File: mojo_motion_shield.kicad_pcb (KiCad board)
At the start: 2 copper layers, 63.5 x 78.7 mm, 1 part, among them P1 MOJO

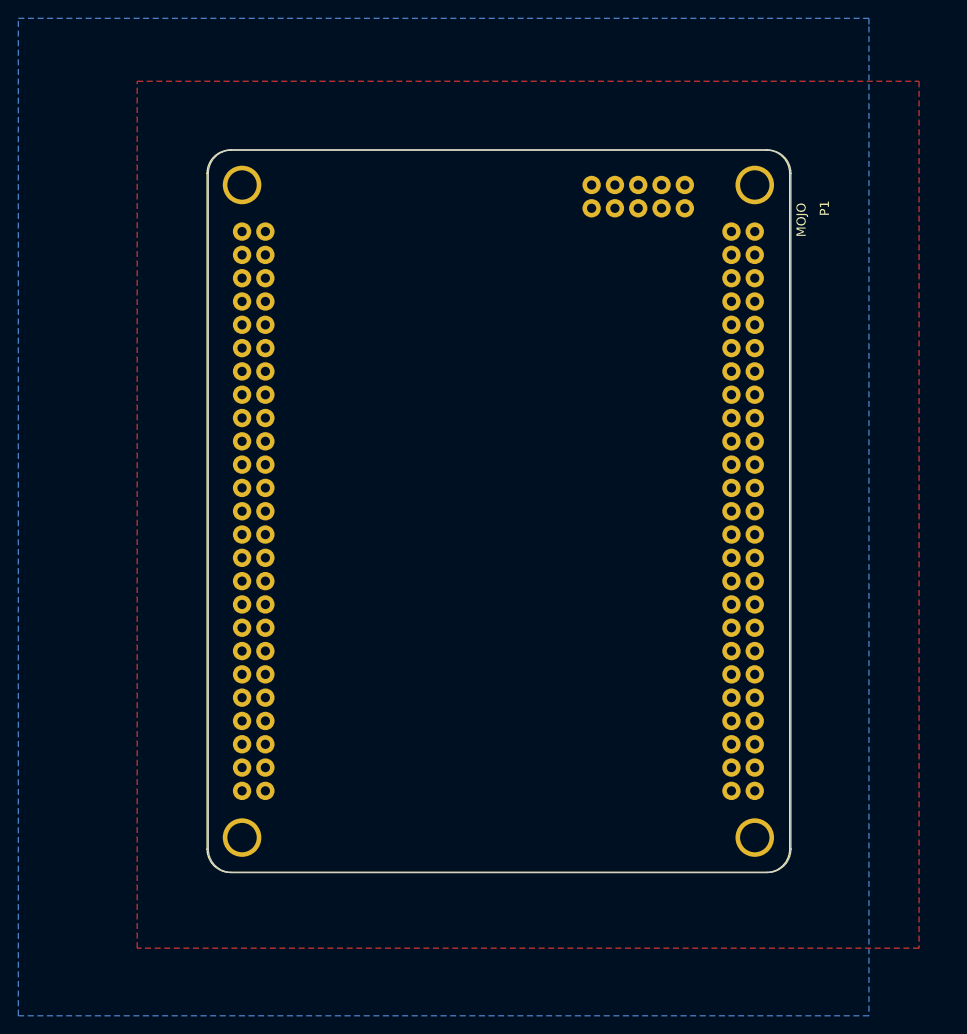
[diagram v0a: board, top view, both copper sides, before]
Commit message: flesh out pcb layout
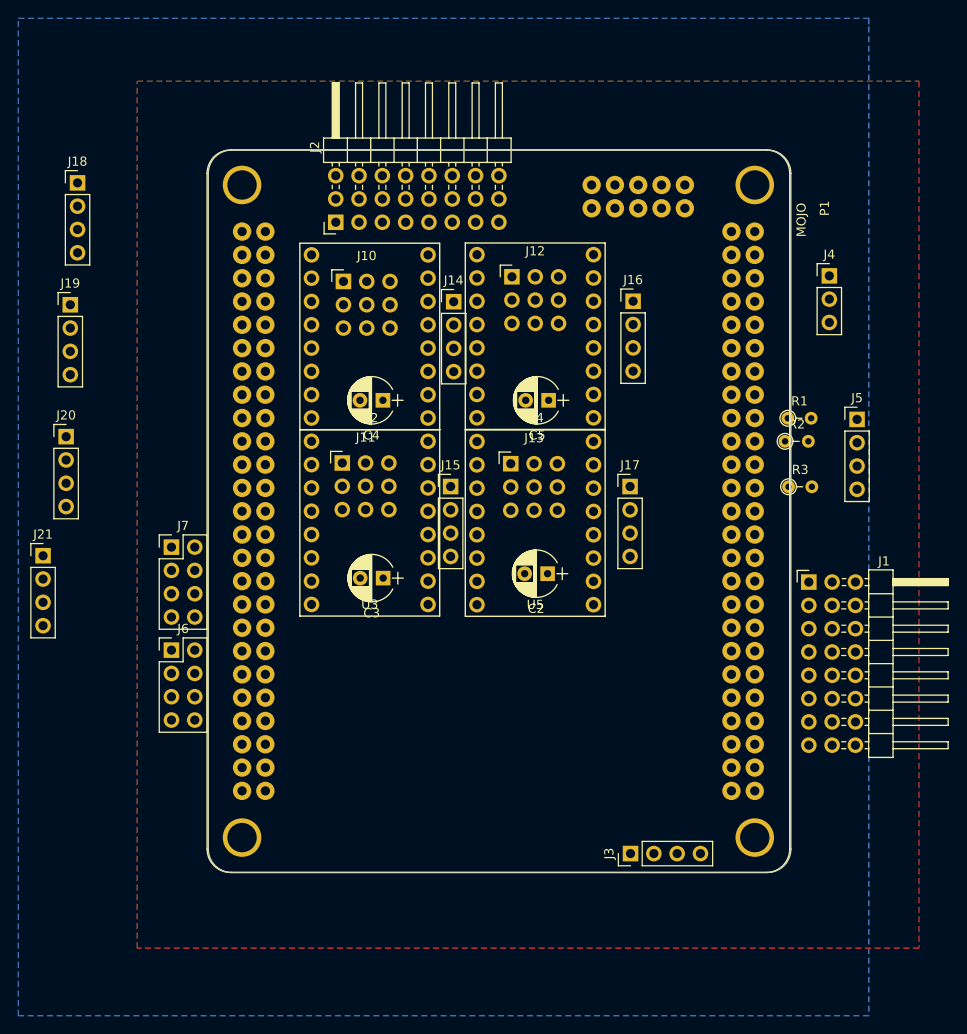
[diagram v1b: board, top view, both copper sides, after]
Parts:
- added C2: CP_Small, Capacitors_THT:CP_Radial_D5.0mm_P2.50mm, F.Cu at (148.7, 105.1)
- added C3: CP_Small, Capacitors_THT:CP_Radial_D5.0mm_P2.50mm, F.Cu at (130.8, 105.6)
- added C4: CP_Small, Capacitors_THT:CP_Radial_D5.0mm_P2.50mm, F.Cu at (130.8, 86.2)
- added C5: CP_Small, Capacitors_THT:CP_Radial_D5.0mm_P2.50mm, F.Cu at (148.9, 86.2)
- added J1: Conn_01x24, mojov3:Pin_Header_Angled_3x08_Pitch2.54mm, F.Cu at (179.8, 106.0)
- added J10: Conn_01x09, mojov3:Pin_Header_Straight_3x03_Pitch2.54mm, F.Cu at (129.0, 73.3)
- added J11: Conn_01x09, mojov3:Pin_Header_Straight_3x03_Pitch2.54mm, F.Cu at (128.9, 93.0)
- added J12: Conn_01x09, mojov3:Pin_Header_Straight_3x03_Pitch2.54mm, F.Cu at (147.4, 72.7)
- added J13: Conn_01x09, mojov3:Pin_Header_Straight_3x03_Pitch2.54mm, F.Cu at (147.3, 93.1)
- added J14: Conn_01x04, Pin_Headers:Pin_Header_Straight_1x04_Pitch2.54mm, F.Cu at (138.5, 75.5)
- added J15: Conn_01x04, Pin_Headers:Pin_Header_Straight_1x04_Pitch2.54mm, F.Cu at (138.2, 95.6)
- added J16: Conn_01x04, Pin_Headers:Pin_Header_Straight_1x04_Pitch2.54mm, F.Cu at (158.1, 75.4)
- added J17: Conn_01x04, Pin_Headers:Pin_Header_Straight_1x04_Pitch2.54mm, F.Cu at (157.7, 95.6)
- added J18: Conn_01x04, Pin_Headers:Pin_Header_Straight_1x04_Pitch2.54mm, F.Cu at (97.5, 62.5)
- added J19: Conn_01x04, Pin_Headers:Pin_Header_Straight_1x04_Pitch2.54mm, F.Cu at (96.7, 75.8)
- added J2: Conn_01x24, mojov3:Pin_Header_Angled_3x08_Pitch2.54mm, F.Cu at (125.7, 64.3)
- added J20: Conn_01x04, Pin_Headers:Pin_Header_Straight_1x04_Pitch2.54mm, F.Cu at (96.3, 90.2)
- added J21: Conn_01x04, Pin_Headers:Pin_Header_Straight_1x04_Pitch2.54mm, F.Cu at (93.8, 103.1)
- added J3: Conn_01x04, Pin_Headers:Pin_Header_Straight_1x04_Pitch2.54mm, F.Cu at (157.8, 135.6)
- added J4: Conn_01x03, Pin_Headers:Pin_Header_Straight_1x03_Pitch2.54mm, F.Cu at (179.5, 72.6)
- added J5: Conn_01x04, Pin_Headers:Pin_Header_Straight_1x04_Pitch2.54mm, F.Cu at (182.5, 88.3)
- added J6: Conn_02x04_Odd_Even, Pin_Headers:Pin_Header_Straight_2x04_Pitch2.54mm, F.Cu at (107.7, 113.4)
- added J7: Conn_02x04_Odd_Even, Pin_Headers:Pin_Header_Straight_2x04_Pitch2.54mm, F.Cu at (107.7, 102.2)
- added R1: R_Small, Resistors_THT:R_Axial_DIN0204_L3.6mm_D1.6mm_P2.54mm_Vertical, F.Cu at (174.9, 88.2)
- added R2: R_Small, Resistors_THT:R_Axial_DIN0204_L3.6mm_D1.6mm_P2.54mm_Vertical, F.Cu at (174.6, 90.7)
- added R3: R_Small, Resistors_THT:R_Axial_DIN0204_L3.6mm_D1.6mm_P2.54mm_Vertical, F.Cu at (175.0, 95.6)
- added U2: A4988, mojov3:A4988, F.Cu at (129.4, 79.2)
- added U3: A4988, mojov3:A4988, F.Cu at (129.4, 99.6)
- added U4: A4988, mojov3:A4988, F.Cu at (147.4, 79.2)
- added U5: A4988, mojov3:A4988, F.Cu at (147.4, 99.6)
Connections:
- P1 pad +V: Net-(P1-Pad+V) -> +3V3
- P1 pad 100: (no net) -> /AENCB
- P1 pad 102: (no net) -> /ASTEP
- P1 pad 105: (no net) -> /ADIR
- P1 pad 112: (no net) -> /ZSTEP
- P1 pad 115: (no net) -> /ZDIR
- P1 pad 116: (no net) -> /CS0
- P1 pad 117: (no net) -> /MOSI
- P1 pad 118: (no net) -> /CS1
- P1 pad 119: (no net) -> /MISO
- P1 pad 120: (no net) -> /CS2
- P1 pad 121: (no net) -> /SCK
- P1 pad 137: (no net) -> /PWM6
- P1 pad 138: (no net) -> /PWM7
- P1 pad 139: (no net) -> /PWM4
- P1 pad 140: (no net) -> /PWM5
- P1 pad 141: (no net) -> /PWM2
- P1 pad 142: (no net) -> /PWM3
- P1 pad 143: (no net) -> /PWM0
- P1 pad 144: (no net) -> /PWM1
- P1 pad 15: (no net) -> Net-(P1-Pad15)
- P1 pad 17: (no net) -> Net-(J5-Pad3)
- P1 pad 22: (no net) -> Net-(P1-Pad22)
- P1 pad 24: (no net) -> Net-(P1-Pad24)
- P1 pad 58: (no net) -> /YENCB
- P1 pad 67: (no net) -> /YENCA
- P1 pad 75: (no net) -> /XENCB
- P1 pad 79: (no net) -> /XENCA
- P1 pad 81: (no net) -> /XSTEP
- P1 pad 83: (no net) -> /XDIR
- P1 pad 85: (no net) -> /YSTEP
- P1 pad 88: (no net) -> /YDIR
- P1 pad 93: (no net) -> /ZENCB
- P1 pad 95: (no net) -> /ZENCA
- P1 pad 98: (no net) -> /AENCA
- P1 pad A0: (no net) -> /A0
- P1 pad A1: (no net) -> /A1
- P1 pad A4: (no net) -> /A4
- P1 pad A5: (no net) -> /A5
- P1 pad A6: (no net) -> /A6
- P1 pad A7: (no net) -> /A7
- P1 pad A8: (no net) -> /A8
- P1 pad A9: (no net) -> /A9
- P1 pad AREF: (no net) -> /AREF
- P1 pad GND: Net-(P1-PadGND) -> GND
- P1 pad RAW: Net-(P1-PadRAW) -> +5V
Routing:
- added copper zone on B.Cu, net GND
- added copper zone on F.Cu, net GND
- removed copper zone on B.Cu, net Net-(P1-PadGND)
- removed copper zone on F.Cu, net Net-(P1-PadGND)

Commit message: implement most of the routes
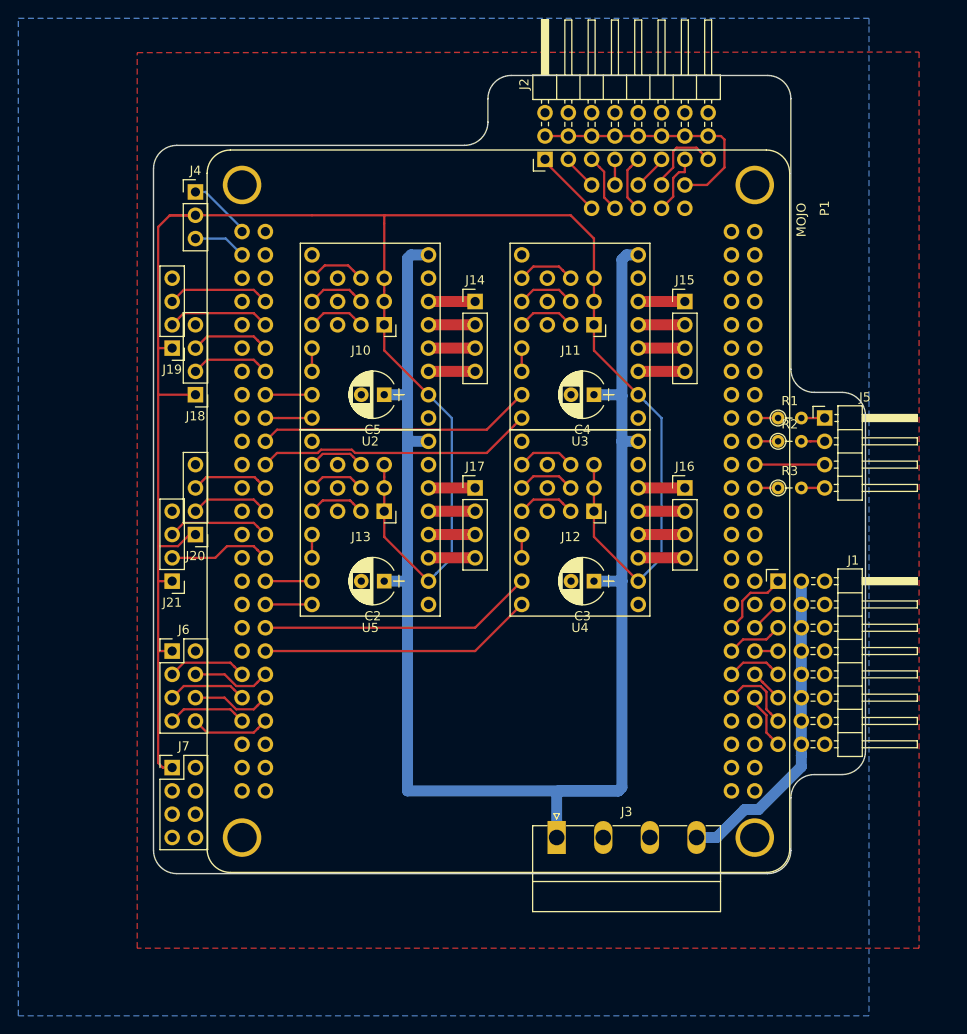
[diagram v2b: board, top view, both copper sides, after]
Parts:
- C2, C3, C4, C5: value CP_Small -> 100uf
- J1: value Conn_01x24 -> SERVO
- J10, J11, J12, J13: value Conn_01x09 -> MSX
- J14, J15, J16, J17: value Conn_01x04 -> MOT
- J18, J19, J20, J21: value Conn_01x04 -> ENC
- J2: value Conn_01x24 -> ANALOG
- J3: value Conn_01x04 -> POWER; footprint Pin_Headers:Pin_Header_Straight_1x04_Pitch2.54mm -> mojov3:PhoenixContact_MC-G_04x5.08mm_Angled
- J4: value Conn_01x03 -> LVSEL
- J5: value Conn_01x04 -> HOST; footprint Pin_Headers:Pin_Header_Straight_1x04_Pitch2.54mm -> Pin_Headers:Pin_Header_Angled_1x04_Pitch2.54mm
- J6: value Conn_02x04_Odd_Even -> SPI0
- J7: value Conn_02x04_Odd_Even -> SPI1
- R1, R2, R3: value R_Small -> 80 Ohm
- moved J4 69.7 mm to (110.4, 63.5)
- moved J15 32.5 mm to (163.7, 75.4)
- moved U3 30.6 mm to (152.3, 79.2)
- moved J11 27.0 mm to (151.3, 78.0), turned to 180 degrees
- moved J18 26.4 mm to (110.4, 85.6), turned to 180 degrees
- moved J12 25.8 mm to (151.3, 98.3), turned to 180 degrees
- moved J7 24.0 mm to (107.8, 126.2)
- moved J2 23.8 mm to (148.5, 57.4)
- moved C4 23.0 mm to (153.8, 85.6)
- moved C3 23.0 mm to (153.8, 105.9)
- moved J16 21.1 mm to (163.7, 95.8)
- moved U4 20.9 mm to (152.3, 99.6)
- moved J13 19.6 mm to (128.4, 98.3), turned to 180 degrees
- moved U5 18.0 mm to (129.4, 99.6)
- moved C5 17.9 mm to (130.9, 85.6)
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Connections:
- J10 pad 1: GND -> /LVTTL
- J10 pad 2: GND -> /LVTTL
- J10 pad 3: GND -> /LVTTL
- J10 pad 7: /LVTTL -> GND
- J10 pad 8: /LVTTL -> GND
- J10 pad 9: /LVTTL -> GND
- J11 pad 1: GND -> /LVTTL
- J11 pad 2: GND -> /LVTTL
- J11 pad 3: GND -> /LVTTL
- J11 pad 7: /LVTTL -> GND
- J11 pad 8: /LVTTL -> GND
- J11 pad 9: /LVTTL -> GND
- J12 pad 1: GND -> /LVTTL
- J12 pad 2: GND -> /LVTTL
- J12 pad 3: GND -> /LVTTL
- J12 pad 7: /LVTTL -> GND
- J12 pad 8: /LVTTL -> GND
- J12 pad 9: /LVTTL -> GND
- J13 pad 1: GND -> /LVTTL
- J13 pad 2: GND -> /LVTTL
- J13 pad 3: GND -> /LVTTL
- J13 pad 7: /LVTTL -> GND
- J13 pad 8: /LVTTL -> GND
- J13 pad 9: /LVTTL -> GND
- J3 pad 1: /EXTPWR -> +12V
- J3 pad 3: +12V -> GND
- J3 pad 4: GND -> /EXTPWR
- P1 pad 100: /AENCB -> /AENCA
- P1 pad 98: /AENCA -> /AENCB
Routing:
- net /LVTTL: track 0.00 -> 240.1 mm
- net +12V: track 0.00 -> 170.4 mm
- net /EXTPWR: track 0.00 -> 34.8 mm
- net /YDIR: track 0.00 -> 30.3 mm
- net /YSTEP: track 0.00 -> 30.0 mm
- net /ZSTEP: track 0.00 -> 30.0 mm
- net /ZDIR: track 0.00 -> 30.0 mm
- net /AREF: track 0.00 -> 27.9 mm
- net /AENCA: track 0.00 -> 11.2 mm
- net /YENCA: track 0.00 -> 11.2 mm
- net /YENCB: track 0.00 -> 11.2 mm
- net /AENCB: track 0.00 -> 11.2 mm
- net /A9: track 0.00 -> 8.70 mm
- net /XENCA: track 0.00 -> 8.67 mm
- net /MISO: track 0.00 -> 8.67 mm
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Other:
- board size 63.5 x 78.7 mm -> 77.6 x 87 mm

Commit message: update 6xTB67S249FTG shield
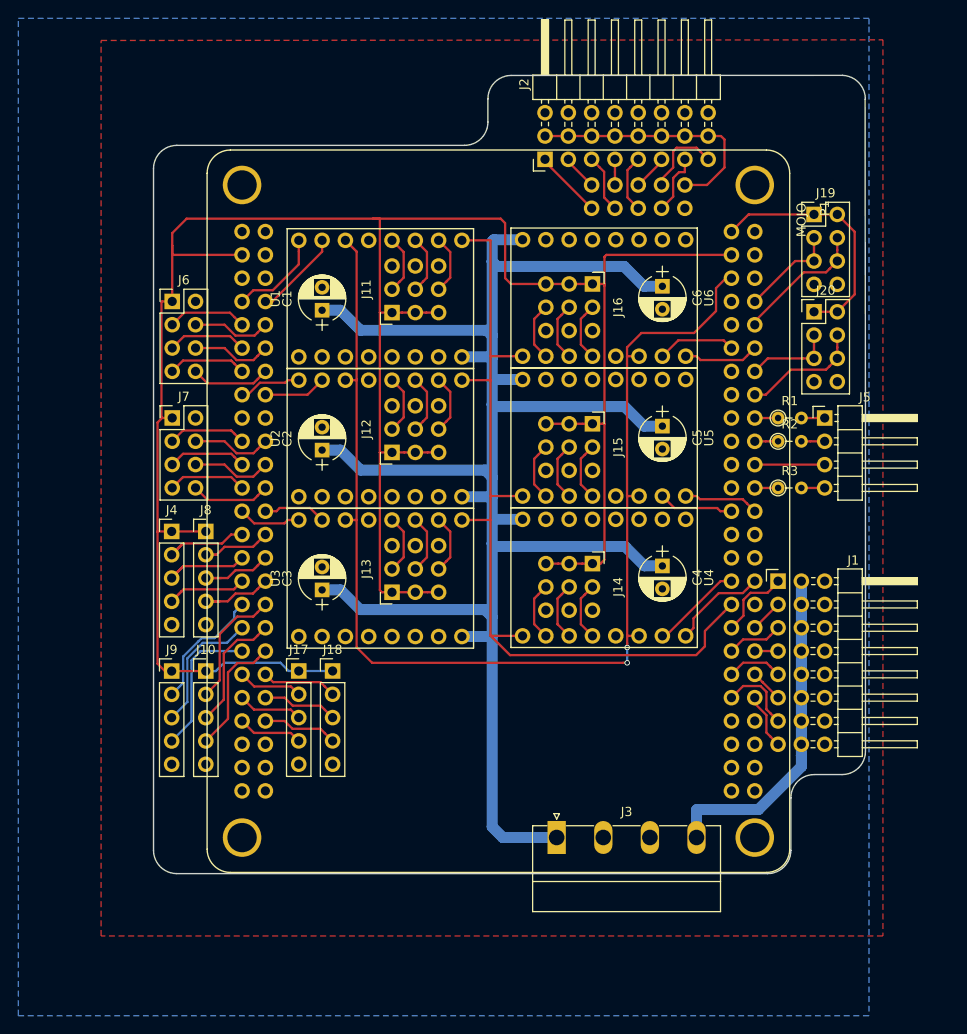
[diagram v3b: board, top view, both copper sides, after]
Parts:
- removed J21: ENC, Pin_Headers:Pin_Header_Straight_1x04_Pitch2.54mm
- added C1: 100uf, Capacitors_THT:CP_Radial_D5.0mm_P2.50mm, F.Cu at (124.2, 76.4)
- added C6: 100uf, Capacitors_THT:CP_Radial_D5.0mm_P2.50mm, F.Cu at (161.3, 73.8)
- added J8: ENC, Connector_PinHeader_2.54mm:PinHeader_1x05_P2.54mm_Vertical, F.Cu at (111.5, 100.5)
- added J9: ENC, Connector_PinHeader_2.54mm:PinHeader_1x05_P2.54mm_Vertical, F.Cu at (107.8, 115.7)
- added U1: TB67S2X9FTG, mojov3:TB67S2X9FTG, F.Cu at (130.5, 75.1)
- added U6: TB67S2X9FTG, mojov3:TB67S2X9FTG, F.Cu at (154.9, 75.1)
- J10: value MSX -> ENC; footprint mojov3:Pin_Header_Straight_3x03_Pitch2.54mm -> Connector_PinHeader_2.54mm:PinHeader_1x05_P2.54mm_Vertical
- J14, J15, J16: value MOT -> MSX; footprint Pin_Headers:Pin_Header_Straight_1x04_Pitch2.54mm -> mojov3:Pin_Header_Straight_3x03_Pitch2.54mm
- J17: value MOT -> ENC; footprint Pin_Headers:Pin_Header_Straight_1x04_Pitch2.54mm -> Connector_PinHeader_2.54mm:PinHeader_1x05_P2.54mm_Vertical
- J18: footprint Pin_Headers:Pin_Header_Straight_1x04_Pitch2.54mm -> Connector_PinHeader_2.54mm:PinHeader_1x05_P2.54mm_Vertical
- J19: value ENC -> SSERIAL0; footprint Pin_Headers:Pin_Header_Straight_1x04_Pitch2.54mm -> Connector_PinHeader_2.54mm:PinHeader_2x04_P2.54mm_Vertical
- J20: value ENC -> SSERIAL1; footprint Pin_Headers:Pin_Header_Straight_1x04_Pitch2.54mm -> Connector_PinHeader_2.54mm:PinHeader_2x04_P2.54mm_Vertical
- J4: value LVSEL -> ENC; footprint Pin_Headers:Pin_Header_Straight_1x03_Pitch2.54mm -> Connector_PinHeader_2.54mm:PinHeader_1x05_P2.54mm_Vertical
- U2, U3, U4, U5: value A4988 -> TB67S2X9FTG; footprint mojov3:A4988 -> mojov3:TB67S2X9FTG
- moved J20 71.7 mm to (177.8, 76.6), turned to 0 degrees
- moved J19 71.5 mm to (177.8, 66.0), turned to 0 degrees
- moved J10 41.4 mm to (111.5, 115.7), turned to 0 degrees
- moved J7 38.1 mm to (107.8, 88.1)
- moved J6 38.1 mm to (107.8, 75.4)
- moved J4 37.1 mm to (107.8, 100.5)
- moved U3 34.2 mm to (130.5, 105.6), turned to 270 degrees
- moved J14 33.6 mm to (153.6, 106.5), turned to 270 degrees
- moved J18 33.6 mm to (125.3, 115.7), turned to 0 degrees
- moved C5 30.5 mm to (161.3, 89.0), turned to 270 degrees
- moved C3 29.6 mm to (124.2, 106.9), turned to 90 degrees
- moved J17 27.7 mm to (121.6, 115.7)
- moved U5 27.1 mm to (154.9, 90.3), turned to 90 degrees
- moved J16 22.1 mm to (153.6, 76.1), turned to 270 degrees
- moved J12 21.4 mm to (131.8, 89.3), turned to 90 degrees
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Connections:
- J10 pad 1: /LVTTL -> +3V3
- J10 pad 2: /LVTTL -> /AENC_A
- J10 pad 3: /LVTTL -> /AENC_B
- J10 pad 4: Net-(J10-Pad4) -> /AENC_I
- J10 pad 5: Net-(J10-Pad5) -> GND
- J11 pad 1: /LVTTL -> +3V3
- J11 pad 2: /LVTTL -> +3V3
- J11 pad 3: /LVTTL -> +3V3
- J12 pad 1: /LVTTL -> +3V3
- J12 pad 2: /LVTTL -> +3V3
- J12 pad 3: /LVTTL -> +3V3
- J13 pad 1: /LVTTL -> +3V3
- J13 pad 2: /LVTTL -> +3V3
- J13 pad 3: /LVTTL -> +3V3
- J14 pad 1: Net-(J14-Pad1) -> +3V3
- J14 pad 2: Net-(J14-Pad2) -> +3V3
- J14 pad 3: Net-(J14-Pad3) -> +3V3
- J15 pad 1: Net-(J15-Pad1) -> +3V3
- J15 pad 2: Net-(J15-Pad2) -> +3V3
- J15 pad 3: Net-(J15-Pad3) -> +3V3
- J16 pad 1: Net-(J16-Pad1) -> +3V3
- J16 pad 2: Net-(J16-Pad2) -> +3V3
- J16 pad 3: Net-(J16-Pad3) -> +3V3
- J17 pad 1: Net-(J17-Pad1) -> +3V3
- J17 pad 2: Net-(J17-Pad2) -> /BENC_A
- J17 pad 3: Net-(J17-Pad3) -> /BENC_B
- J17 pad 4: Net-(J17-Pad4) -> /BENC_I
- J18 pad 1: /LVTTL -> +3V3
- J18 pad 2: /XENCA -> /CENC_A
- J18 pad 3: /XENCB -> /CENC_B
- J18 pad 4: GND -> /CENC_I
- J19 pad 1: /LVTTL -> +5V
- J19 pad 2: /YENCA -> +5V
- J19 pad 3: /YENCB -> /SS0TX
- J19 pad 4: GND -> /SS0RX
- J20 pad 1: /LVTTL -> +5V
- J20 pad 2: /ZENCA -> +5V
- J20 pad 3: /ZENCB -> /SS1TX
- J20 pad 4: GND -> /SS1RX
- J4 pad 1: +5V -> +3V3
- J4 pad 2: /LVTTL -> /XENC_A
- J4 pad 3: +3V3 -> /XENC_B
- J6 pad 1: /LVTTL -> +3V3
- J6 pad 4: /MOSI -> /SPI0_OUT
- J6 pad 6: /MISO -> /SPI0_IN
- J6 pad 8: /SCK -> /SPI0_CLK
- J7 pad 1: /LVTTL -> +3V3
- J7 pad 3: (no net) -> /CS3
- J7 pad 4: (no net) -> /SPI1_OUT
- J7 pad 5: (no net) -> /CS4
- J7 pad 6: (no net) -> /SPI1_IN
- J7 pad 7: (no net) -> /CS5
- J7 pad 8: (no net) -> /SPI1_CLK
- P1 pad 1: (no net) -> /~MOTION
- P1 pad 100: /AENCA -> /YENC_B
- P1 pad 101: (no net) -> /XENC_I
- P1 pad 102: /ASTEP -> /YENC_I
- P1 pad 104: (no net) -> /ZENC_A
- P1 pad 105: /ADIR -> /AENC_A
- P1 pad 11: (no net) -> /BSTEP
- P1 pad 111: (no net) -> /ZENC_B
- P1 pad 112: /ZSTEP -> /AENC_B
- P1 pad 114: (no net) -> /ZENC_I
- P1 pad 115: /ZDIR -> /AENC_I
- P1 pad 116: /CS0 -> /BENC_A
- P1 pad 117: /MOSI -> /CENC_A
- P1 pad 118: /CS1 -> /BENC_B
- P1 pad 119: /MISO -> /CENC_B
- P1 pad 12: (no net) -> /BDIR
- P1 pad 120: /CS2 -> /BENC_I
- P1 pad 121: /SCK -> /CENC_I
- P1 pad 27: (no net) -> /SS1RX
- P1 pad 30: (no net) -> /SS1TX
- P1 pad 32: (no net) -> /CSTEP
- P1 pad 33: (no net) -> /CDIR
- P1 pad 35: (no net) -> /SS0RX
- P1 pad 41: (no net) -> /SS0TX
- P1 pad 5: (no net) -> /ASTEP
- P1 pad 50: (no net) -> /~ECO
- P1 pad 57: (no net) -> /XDIR
- P1 pad 58: /YENCB -> /XSTEP
- P1 pad 6: (no net) -> /ADIR
- P1 pad 66: (no net) -> /CS0
- P1 pad 67: /YENCA -> /SPI0_OUT
- P1 pad 74: (no net) -> /CS1
- P1 pad 75: /XENCB -> /SPI0_IN
- P1 pad 78: (no net) -> /CS2
- P1 pad 79: /XENCA -> /SPI0_CLK
- P1 pad 80: (no net) -> /YDIR
- P1 pad 81: /XSTEP -> /YSTEP
- P1 pad 83: /XDIR -> (no net)
- P1 pad 84: (no net) -> /CS3
- P1 pad 85: /YSTEP -> /SPI1_OUT
- P1 pad 87: (no net) -> /CS4
- P1 pad 88: /YDIR -> /SPI1_IN
- P1 pad 92: (no net) -> /CS5
- P1 pad 93: /ZENCB -> /SPI1_CLK
- P1 pad 94: (no net) -> /ZDIR
- P1 pad 95: /ZENCA -> /ZSTEP
- P1 pad 97: (no net) -> /XENC_A
- P1 pad 98: /AENCB -> /YENC_A
- P1 pad 99: (no net) -> /XENC_B
- U2 pad 1: (no net) -> /~MOTION
- U2 pad 11: Net-(J14-Pad1) -> (no net)
- U2 pad 12: Net-(J14-Pad2) -> (no net)
- U2 pad 13: Net-(J14-Pad3) -> (no net)
- U2 pad 14: Net-(J14-Pad4) -> (no net)
- U2 pad 15: /LVTTL -> (no net)
- U2 pad 2: Net-(J10-Pad6) -> Net-(J12-Pad6)
- U2 pad 3: Net-(J10-Pad5) -> Net-(J12-Pad5)
- U2 pad 4: Net-(J10-Pad4) -> Net-(J12-Pad4)
- U2 pad 5: Net-(U2-Pad5) -> (no net)
- U2 pad 6: Net-(U2-Pad5) -> /~ECO
- U2 pad 7: /XSTEP -> /YSTEP
- U2 pad 8: /XDIR -> /YDIR
- U3 pad 1: (no net) -> /~MOTION
- U3 pad 11: Net-(J15-Pad1) -> (no net)
- U3 pad 12: Net-(J15-Pad2) -> (no net)
- U3 pad 13: Net-(J15-Pad3) -> (no net)
- U3 pad 14: Net-(J15-Pad4) -> (no net)
- U3 pad 15: /LVTTL -> (no net)
- U3 pad 2: Net-(J11-Pad6) -> Net-(J13-Pad6)
- U3 pad 3: Net-(J11-Pad5) -> Net-(J13-Pad5)
- U3 pad 4: Net-(J11-Pad4) -> Net-(J13-Pad4)
- U3 pad 5: Net-(U3-Pad5) -> (no net)
- U3 pad 6: Net-(U3-Pad5) -> /~ECO
- U3 pad 7: /YSTEP -> /ZSTEP
- U3 pad 8: /YDIR -> /ZDIR
- U4 pad 1: (no net) -> /~MOTION
- U4 pad 11: Net-(J16-Pad1) -> (no net)
- U4 pad 12: Net-(J16-Pad2) -> (no net)
- U4 pad 13: Net-(J16-Pad3) -> (no net)
- U4 pad 14: Net-(J16-Pad4) -> (no net)
- U4 pad 15: /LVTTL -> (no net)
- U4 pad 2: Net-(J12-Pad6) -> Net-(J14-Pad6)
- U4 pad 3: Net-(J12-Pad5) -> Net-(J14-Pad5)
- U4 pad 4: Net-(J12-Pad4) -> Net-(J14-Pad4)
- U4 pad 5: Net-(U4-Pad5) -> (no net)
- U4 pad 6: Net-(U4-Pad5) -> /~ECO
- U4 pad 7: /ZSTEP -> /ASTEP
- U4 pad 8: /ZDIR -> /ADIR
- U5 pad 1: (no net) -> /~MOTION
- U5 pad 11: Net-(J17-Pad1) -> (no net)
- U5 pad 12: Net-(J17-Pad2) -> (no net)
- U5 pad 13: Net-(J17-Pad3) -> (no net)
- U5 pad 14: Net-(J17-Pad4) -> (no net)
- U5 pad 15: /LVTTL -> (no net)
- U5 pad 2: Net-(J13-Pad6) -> Net-(J15-Pad6)
- U5 pad 3: Net-(J13-Pad5) -> Net-(J15-Pad5)
- U5 pad 4: Net-(J13-Pad4) -> Net-(J15-Pad4)
- U5 pad 5: Net-(U5-Pad5) -> (no net)
- U5 pad 6: Net-(U5-Pad5) -> /~ECO
- U5 pad 7: /ASTEP -> /BSTEP
- U5 pad 8: /ADIR -> /BDIR
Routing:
- net +3V3: track 5.82 -> 258.1 mm
- net /LVTTL: track 240.1 -> 0.00 mm
- net /~ECO: track 0.00 -> 131.9 mm, vias 0 -> 2
- net /~MOTION: track 0.00 -> 93.4 mm
- net +12V: track 170.4 -> 209.3 mm
- net /YDIR: track 30.3 -> 6.84 mm
- net /YSTEP: track 30.0 -> 6.84 mm
- net /ZSTEP: track 30.0 -> 6.87 mm
- net /ZDIR: track 30.0 -> 6.88 mm
- net +5V: track 7.07 -> 27.0 mm
- net /ZENC_I: track 0.00 -> 15.6 mm
- net /SS0RX: track 0.00 -> 14.6 mm
- net /ZENC_B: track 0.00 -> 14.5 mm
- net /ZENC_A: track 0.00 -> 13.8 mm
- net /AENC_I: track 0.00 -> 13.5 mm
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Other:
- outline, holes or cut-outs redrawn

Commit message: route fault pins from drivers to fpga
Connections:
- P1 pad 51: (no net) -> /~FAULT
- U1 pad 15: (no net) -> /~FAULT
- U2 pad 15: (no net) -> /~FAULT
- U3 pad 15: (no net) -> /~FAULT
- U4 pad 15: (no net) -> /~FAULT
- U5 pad 15: (no net) -> /~FAULT
- U6 pad 15: (no net) -> /~FAULT
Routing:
- net /~FAULT: track 0.00 -> 133.7 mm, vias 0 -> 1
- net +3V3: track 258.1 -> 267.9 mm
- net /~ECO: track 131.9 -> 128.5 mm
